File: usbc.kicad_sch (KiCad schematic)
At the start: 9 parts, among them J1 Conn_01x04, J2 USB_C_Receptacle_USB2.0_16P, U1 XC6206PxxxMR, U2 SRV05-4

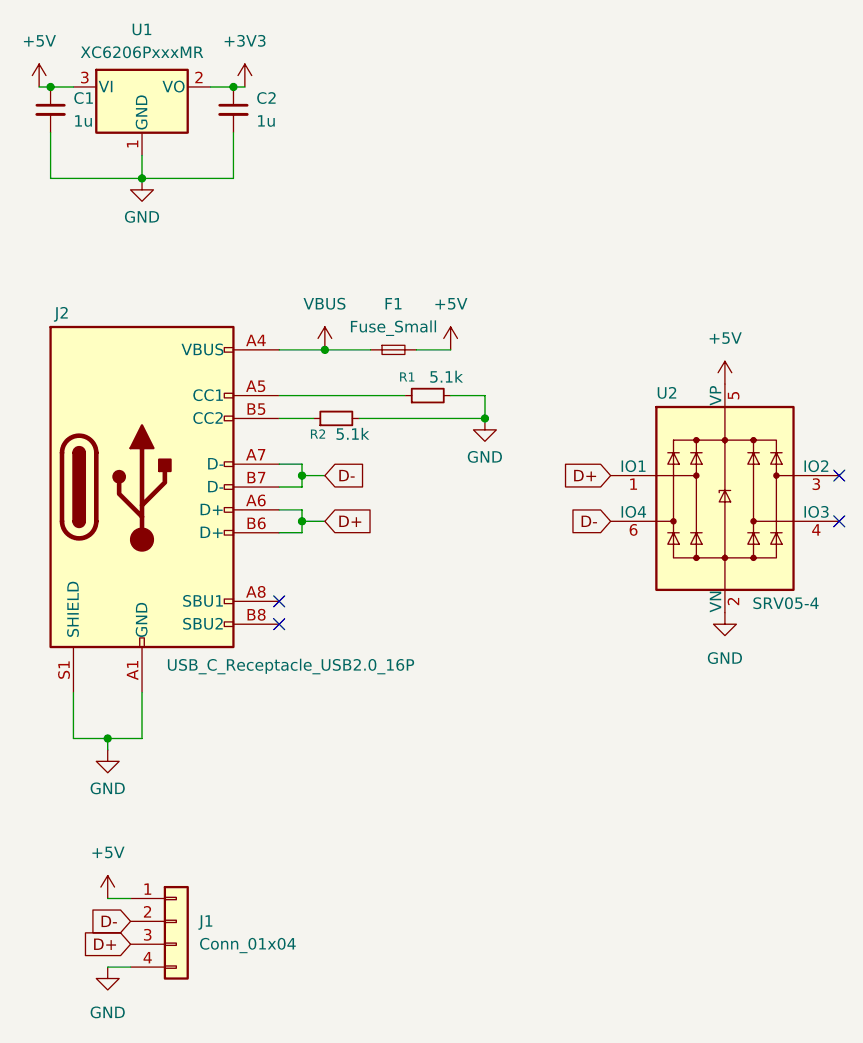
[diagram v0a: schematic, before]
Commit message: 4 layers
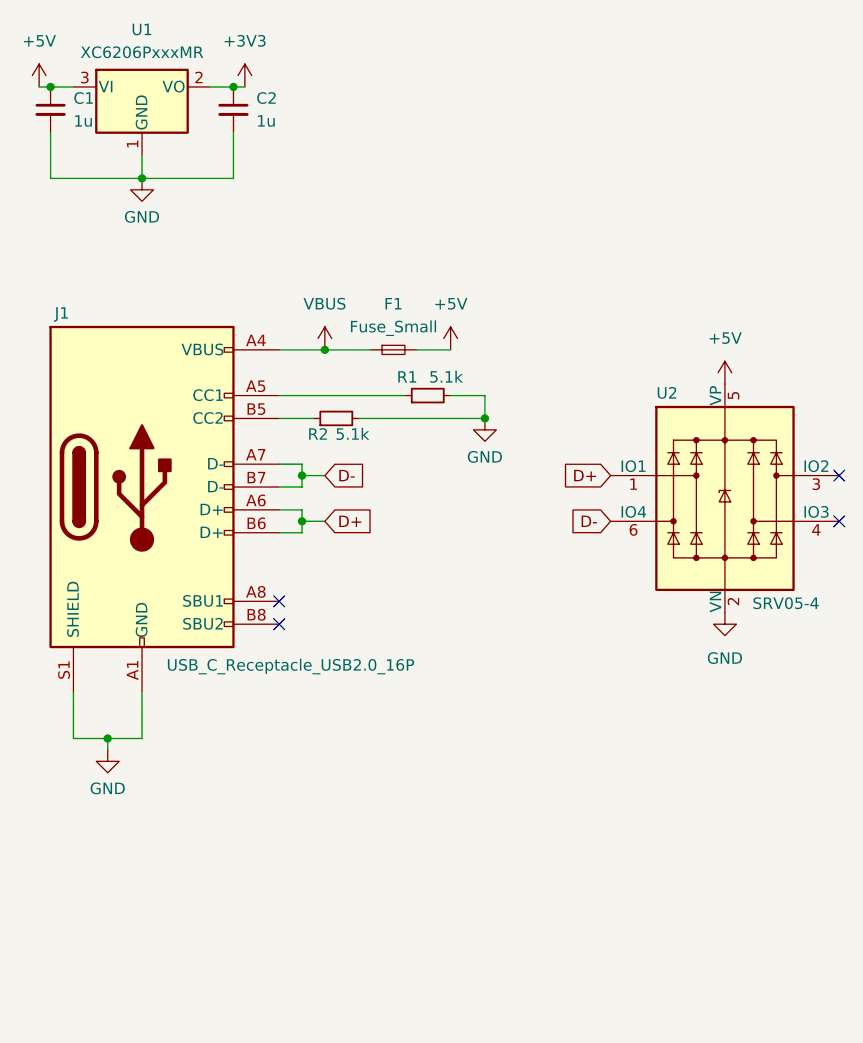
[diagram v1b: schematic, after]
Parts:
- removed J1: Conn_01x04, Library:JST_SH_SM04B-SRSS-TB_1x04-1MP_P1.00mm_Horizontal, symbol Connector_Generic:Conn_01x04
- renumbered J2 to J1

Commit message: BOM
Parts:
- C1, C2: LCSC (none) -> C14445
- F1: LCSC (none) -> C99563
- J1: LCSC (none) -> C5370443
- R1, R2: LCSC (none) -> C25905
- U1: LCSC (none) -> C5446
- U2: LCSC (none) -> C7519
